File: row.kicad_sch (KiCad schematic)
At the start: 3 parts

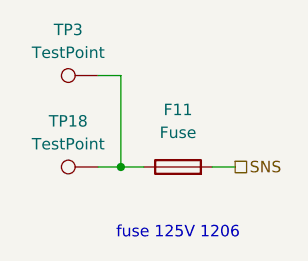
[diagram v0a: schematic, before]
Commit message: Change last end to 0 from 17
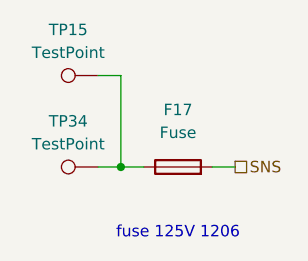
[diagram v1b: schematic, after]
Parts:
- renumbered F11 to F17, TP3 to TP15, TP18 to TP34
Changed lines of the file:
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@@
 		(dnp no)
 		(fields_autoplaced yes)
-		(property "Reference" "F11"
+		(property "Reference" "F17"
 			(at 72.39 54.61 90)
 			(effects
@@
 		(dnp no)
 		(fields_autoplaced yes)
-		(property "Reference" "TP18"
+		(property "Reference" "TP34"
 			(at 60.198 55.88 90)
 			(effects
@@
 		(dnp no)
 		(fields_autoplaced yes)
-		(property "Reference" "TP3"
+		(property "Reference" "TP15"
 			(at 60.198 45.72 90)
 			(effects
